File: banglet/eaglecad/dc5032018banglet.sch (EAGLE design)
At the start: 41 parts, among them Q3 DMG3415U-7, U2 AP2112(3.3V), U3 MCP73831T-2ACI/OT, U4 CP2104, X1 32.768, X2 JSTPH, X4 20329

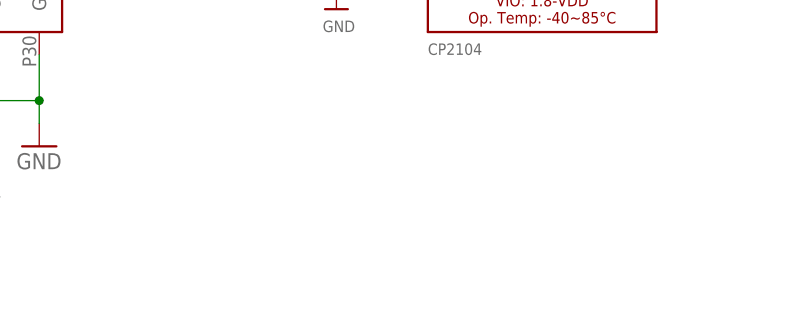
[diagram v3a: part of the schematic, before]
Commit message: add 2 fiducials
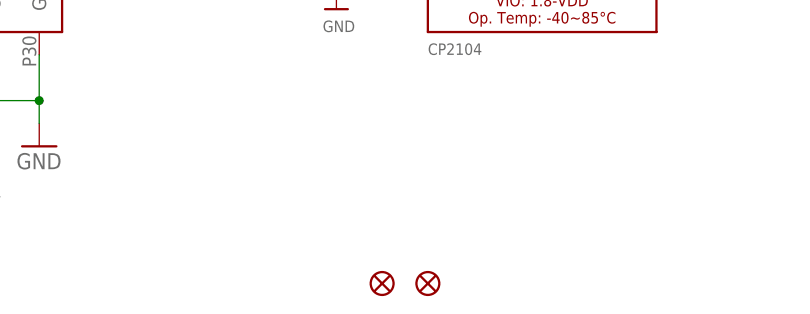
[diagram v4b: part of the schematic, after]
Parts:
- added FD1, FD2: FIDUCIALUFIDUCIAL, SparkFun-Aesthetics:FIDUCIALUFIDUCIAL
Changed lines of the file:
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@@
 <part name="C4" library="SparkFun-Capacitors" library_urn="urn:adsk.eagle:library:510" deviceset="22PF" device="-0603-50V-5%" package3d_urn="urn:adsk.eagle:package:37414/1" value="22pF"/>
 <part name="C2" library="SparkFun-Capacitors" library_urn="urn:adsk.eagle:library:510" deviceset="22PF" device="-0603-50V-5%" package3d_urn="urn:adsk.eagle:package:37414/1" value="22pF"/>
+<part name="FD1" library="SparkFun-Aesthetics" library_urn="urn:adsk.eagle:library:507" deviceset="FIDUCIAL" device="UFIDUCIAL" package3d_urn="urn:adsk.eagle:package:37111/1"/>
+<part name="FD2" library="SparkFun-Aesthetics" library_urn="urn:adsk.eagle:library:507" deviceset="FIDUCIAL" device="UFIDUCIAL" package3d_urn="urn:adsk.eagle:package:37111/1"/>
 </parts>
 <sheets>
@@
 <instance part="C4" gate="G$1" x="-48.26" y="-27.94"/>
 <instance part="C2" gate="G$1" x="-33.02" y="-27.94"/>
+<instance part="FD1" gate="G$1" x="60.96" y="-60.96"/>
+<instance part="FD2" gate="G$1" x="66.04" y="-60.96"/>
 </instances>
 <busses>

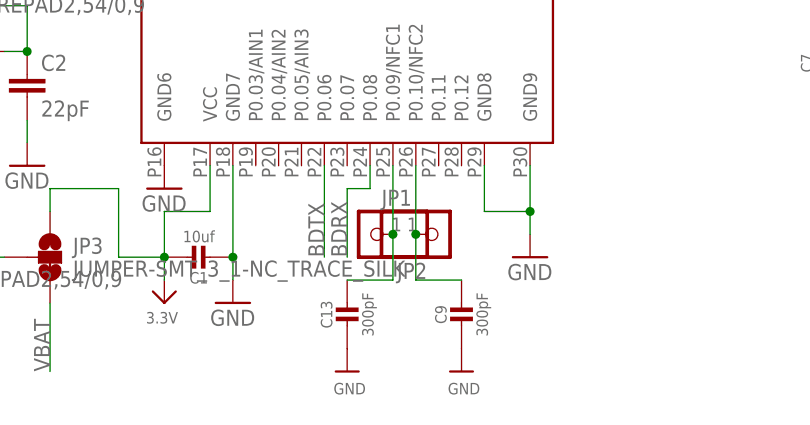
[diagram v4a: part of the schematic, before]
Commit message: removed NFC parts; deleted stray silk
silk still a mess.  I *think* I got all the stray labels.
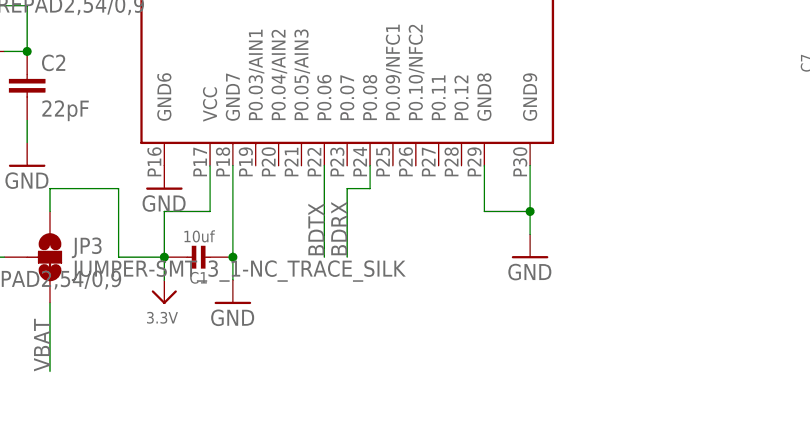
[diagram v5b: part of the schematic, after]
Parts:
- removed C13, C9: 300pF, microbuilder:CAP_CERAMIC_0603MP
- removed JP1, JP2: (no value), microbuilder:HEADER-1X12MM
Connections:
- removed net N$6: C9.1, JP1.1, U1.P0.10/NFC2
- removed net P0.09/NFC1: C13.1, JP2.1, U1.P0.09/NFC1
- net GND: no longer C13.2, C9.2
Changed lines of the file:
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@@
 <part name="GND8" library="supply1" library_urn="urn:adsk.eagle:library:371" deviceset="GND" device=""/>
 <part name="X1" library="adafruit2" deviceset="XTAL" device="-3.2X1.5" value="32.768"/>
-<part name="JP1" library="microbuilder" deviceset="HEADER-1X1" device="2MM"/>
-<part name="JP2" library="microbuilder" deviceset="HEADER-1X1" device="2MM"/>
-<part name="C9" library="microbuilder" deviceset="CAP_CERAMIC" device="_0603MP" value="300pF"/>
-<part name="C13" library="microbuilder" deviceset="CAP_CERAMIC" device="_0603MP" value="300pF"/>
-<part name="U$23" library="microbuilder" deviceset="GND" device=""/>
-<part name="U$28" library="microbuilder" deviceset="GND" device=""/>
 <part name="GND14" library="supply1" library_urn="urn:adsk.eagle:library:371" deviceset="GND" device=""/>
 <part name="GND15" library="supply1" library_urn="urn:adsk.eagle:library:371" deviceset="GND" device=""/>
@@
 <instance part="GND8" gate="1" x="-33.02" y="-35.56"/>
 <instance part="X1" gate="G$1" x="-40.64" y="-22.86"/>
-<instance part="JP1" gate="G$1" x="12.7" y="-43.18"/>
-<instance part="JP2" gate="G$1" x="5.08" y="-43.18" rot="R180"/>
-<instance part="C9" gate="G$1" x="15.24" y="-53.34"/>
-<instance part="C13" gate="G$1" x="2.54" y="-53.34"/>
-<instance part="U$23" gate="G$1" x="2.54" y="-58.42"/>
-<instance part="U$28" gate="G$1" x="15.24" y="-58.42"/>
 <instance part="GND14" gate="1" x="38.1" y="25.4" rot="R90"/>
 <instance part="GND15" gate="1" x="22.86" y="-45.72"/>
@@
 <wire x1="-10.16" y1="-45.72" x2="-10.16" y2="-35.56" width="0.1524" layer="91"/>
 <junction x="-10.16" y="-45.72"/>
-</segment>
-<segment>
-<pinref part="C13" gate="G$1" pin="2"/>
-<pinref part="U$23" gate="G$1" pin="GND"/>
-</segment>
-<segment>
-<pinref part="C9" gate="G$1" pin="2"/>
-<pinref part="U$28" gate="G$1" pin="GND"/>
 </segment>
 <segment>
@@
 </segment>
 </net>
-<net name="P0.09/NFC1" class="0">
-<segment>
-<pinref part="JP2" gate="G$1" pin="1"/>
-<pinref part="C13" gate="G$1" pin="1"/>
-<wire x1="2.54" y1="-48.26" x2="7.62" y2="-48.26" width="0.1524" layer="91"/>
-<wire x1="7.62" y1="-48.26" x2="7.62" y2="-43.18" width="0.1524" layer="91"/>
-<pinref part="U1" gate="G$1" pin="P0.09/NFC1"/>
-<wire x1="7.62" y1="-43.18" x2="7.62" y2="-35.56" width="0.1524" layer="91"/>
-<junction x="7.62" y="-43.18"/>
-</segment>
-</net>
 <net name="TRACED0" class="0">
 <segment>
@@
 </segment>
 </net>
-<net name="N$6" class="0">
-<segment>
-<pinref part="U1" gate="G$1" pin="P0.10/NFC2"/>
-<pinref part="JP1" gate="G$1" pin="1"/>
-<wire x1="10.16" y1="-35.56" x2="10.16" y2="-43.18" width="0.1524" layer="91"/>
-<pinref part="C9" gate="G$1" pin="1"/>
-<wire x1="15.24" y1="-48.26" x2="10.16" y2="-48.26" width="0.1524" layer="91"/>
-<wire x1="10.16" y1="-48.26" x2="10.16" y2="-43.18" width="0.1524" layer="91"/>
-<junction x="10.16" y="-43.18"/>
-</segment>
-</net>

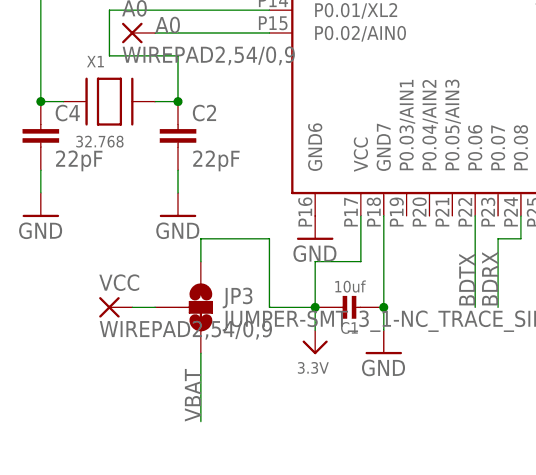
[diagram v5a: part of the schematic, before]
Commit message: make label for LED strip a little clearer
Move two vias away from bmd pads
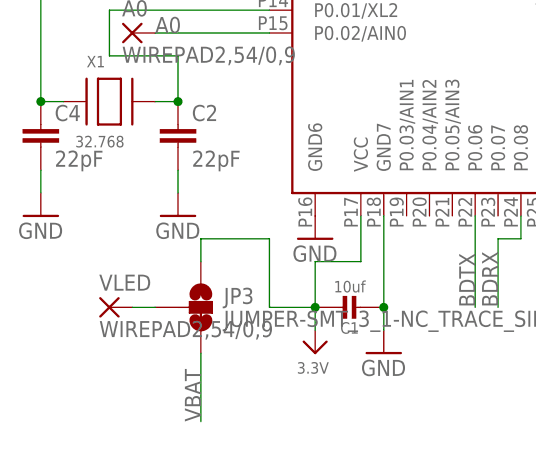
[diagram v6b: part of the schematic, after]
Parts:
- renumbered VCC to VLED
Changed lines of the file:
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@@
 <part name="GND15" library="supply1" library_urn="urn:adsk.eagle:library:371" deviceset="GND" device=""/>
 <part name="A0" library="wirepad" library_urn="urn:adsk.eagle:library:412" deviceset="WIREPAD" device="2,54/0,9"/>
-<part name="VCC" library="wirepad" library_urn="urn:adsk.eagle:library:412" deviceset="WIREPAD" device="2,54/0,9"/>
+<part name="VLED" library="wirepad" library_urn="urn:adsk.eagle:library:412" deviceset="WIREPAD" device="2,54/0,9"/>
 <part name="GND" library="wirepad" library_urn="urn:adsk.eagle:library:412" deviceset="WIREPAD" device="2,54/0,9"/>
 <part name="X4" library="microbuilder" deviceset="MICRO-USB-SMD-B-(10118193-0001LF)-ADASYM" device="" value="20329"/>
@@
 <instance part="GND15" gate="1" x="22.86" y="-45.72"/>
 <instance part="A0" gate="G$1" x="-38.1" y="-15.24"/>
-<instance part="VCC" gate="G$1" x="-40.64" y="-45.72"/>
+<instance part="VLED" gate="G$1" x="-40.64" y="-45.72"/>
 <instance part="GND" gate="G$1" x="-45.72" y="10.16"/>
 <instance part="X4" gate="G$1" x="104.14" y="68.58" rot="R270"/>
@@
 <net name="N$3" class="0">
 <segment>
-<pinref part="VCC" gate="G$1" pin="P"/>
+<pinref part="VLED" gate="G$1" pin="P"/>
 <pinref part="JP3" gate="G$1" pin="2"/>
 <wire x1="-38.1" y1="-45.72" x2="-35.56" y2="-45.72" width="0.1524" layer="91"/>

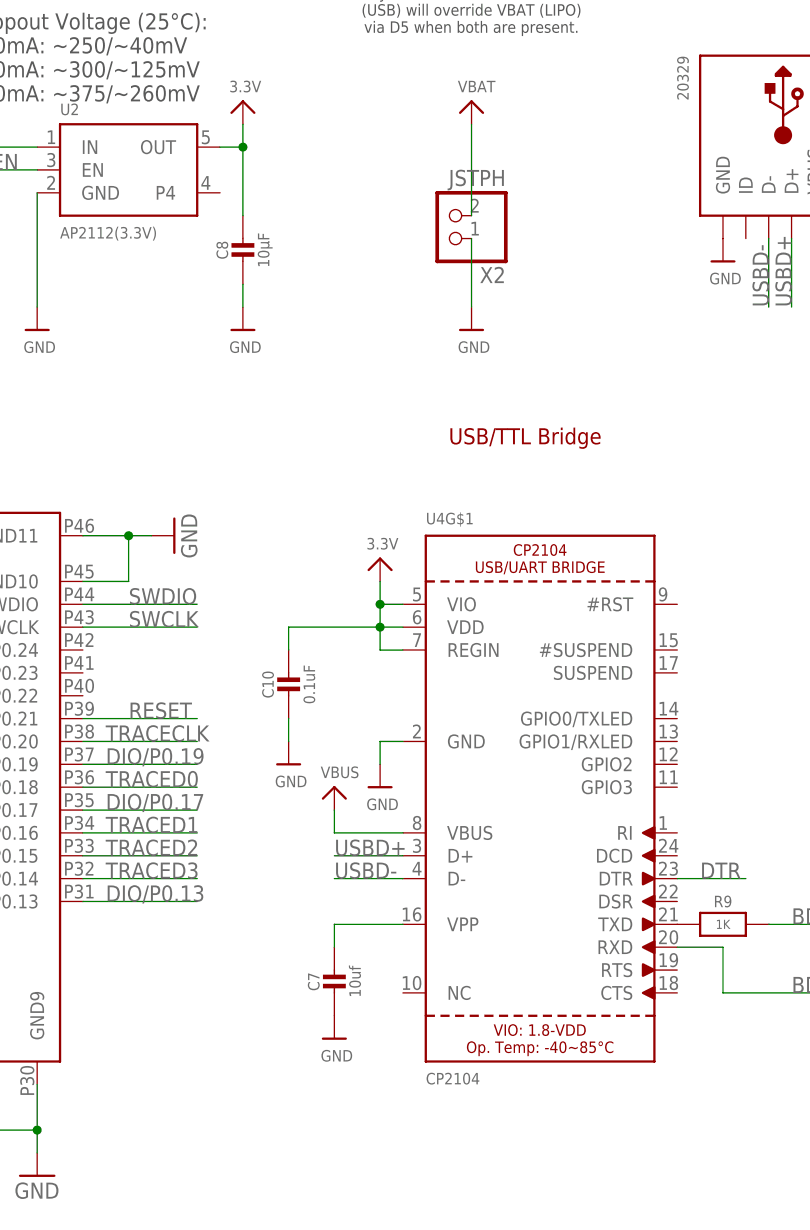
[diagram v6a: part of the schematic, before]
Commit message: Removed cap and replaced JST connector with vias
VPP on the UART is for a one time ROM programming of the UART
which we don't need, so removing it.

We were unable to find batteries that came with the JST female
connectors that went with the used board mounted connector.
Replacing it with vias to use with either board mounted breakaway
header or something else which will fit.

Signed-off-by: nisha <nishakumarx@gmail.com>
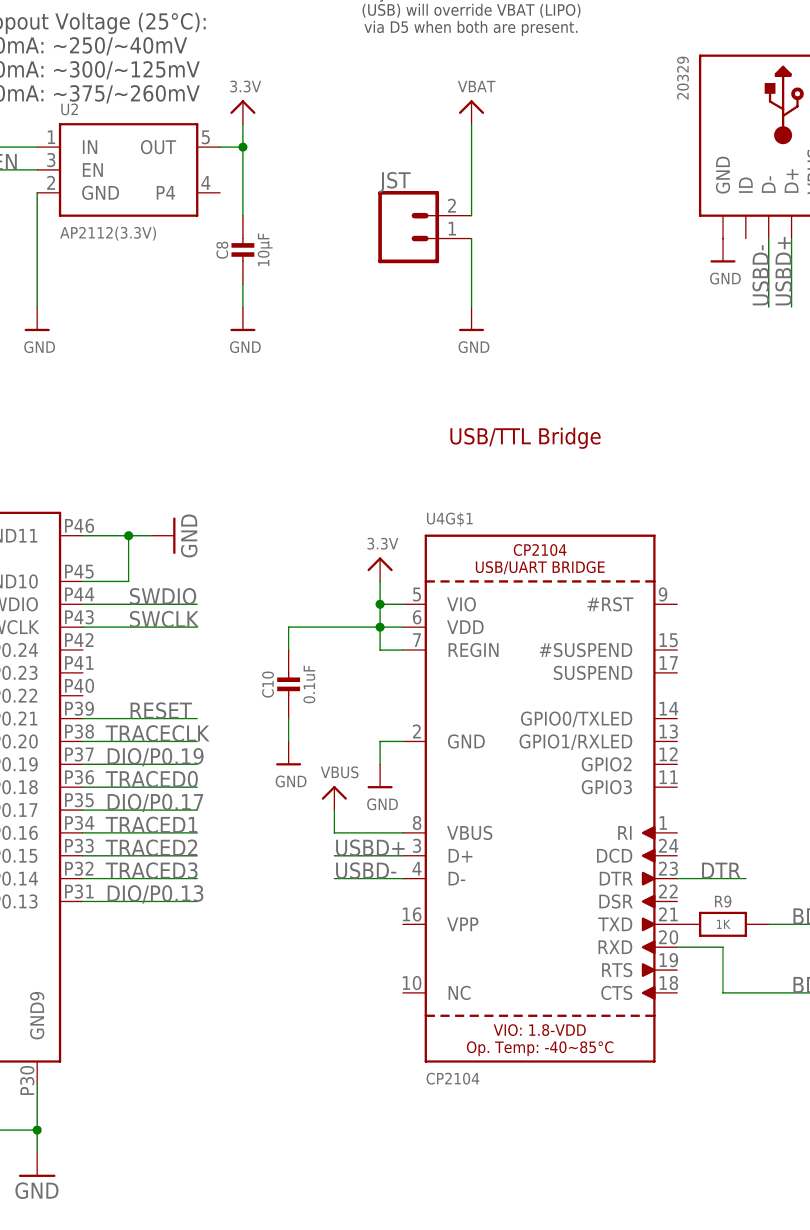
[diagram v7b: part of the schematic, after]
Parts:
- removed C7: 10uf, microbuilder:CAP_CERAMIC0805-NOOUTLINE
- removed X2: JSTPH, microbuilder:CON_JST_PH_2PIN
- added JST: (no value), SparkFun-Connectors:CONN_02
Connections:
- removed net N$14: C7.1, U4G$1.VPP
- net GND: now also JST.1; no longer C7.2, X2.1
- net VBAT: now also JST.2; no longer X2.2
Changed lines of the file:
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@@
 <part name="R12" library="microbuilder" deviceset="RESISTOR" device="_0603_NOOUT" value="100k"/>
 <part name="U$44" library="microbuilder" deviceset="GND" device=""/>
-<part name="X2" library="microbuilder" deviceset="CON_JST_PH_2PIN" device="" value="JSTPH"/>
 <part name="U$16" library="microbuilder" deviceset="VBAT" device=""/>
 <part name="U$22" library="microbuilder" deviceset="GND" device=""/>
@@
 <part name="U$31" library="microbuilder" deviceset="VBUS" device=""/>
 <part name="R9" library="microbuilder" deviceset="RESISTOR" device="_0603_NOOUT" value="1K"/>
-<part name="C7" library="microbuilder" deviceset="CAP_CERAMIC" device="0805-NOOUTLINE" value="10uf"/>
-<part name="U$15" library="microbuilder" deviceset="GND" device=""/>
 <part name="SWD" library="SparkFun-Connectors" deviceset="M04" device="LOCK"/>
 <part name="U1" library="BMD-300" deviceset="BMD-300" device=""/>
@@
 <part name="FD1" library="SparkFun-Aesthetics" library_urn="urn:adsk.eagle:library:507" deviceset="FIDUCIAL" device="UFIDUCIAL" package3d_urn="urn:adsk.eagle:package:37111/1"/>
 <part name="FD2" library="SparkFun-Aesthetics" library_urn="urn:adsk.eagle:library:507" deviceset="FIDUCIAL" device="UFIDUCIAL" package3d_urn="urn:adsk.eagle:package:37111/1"/>
+<part name="JST" library="SparkFun-Connectors" library_urn="urn:adsk.eagle:library:513" deviceset="CONN_02" device="" package3d_urn="urn:adsk.eagle:package:38039/1"/>
 </parts>
 <sheets>
@@
 <instance part="R12" gate="G$1" x="-10.16" y="60.96" rot="R90"/>
 <instance part="U$44" gate="G$1" x="-10.16" y="48.26"/>
-<instance part="X2" gate="G$1" x="68.58" y="60.96" rot="R180"/>
 <instance part="U$16" gate="G$1" x="71.12" y="73.66"/>
 <instance part="U$22" gate="G$1" x="71.12" y="48.26"/>
@@
 <instance part="U$31" gate="G$1" x="55.88" y="-2.54"/>
 <instance part="R9" gate="G$1" x="99.06" y="-17.78"/>
-<instance part="C7" gate="G$1" x="55.88" y="-25.4"/>
-<instance part="U$15" gate="G$1" x="55.88" y="-30.48"/>
 <instance part="SWD" gate="G$1" x="137.16" y="-15.24"/>
 <instance part="U1" gate="G$1" x="2.54" y="7.62"/>
@@
 <instance part="FD1" gate="G$1" x="60.96" y="-60.96"/>
 <instance part="FD2" gate="G$1" x="66.04" y="-60.96"/>
+<instance part="JST" gate="G$1" x="63.5" y="58.42"/>
 </instances>
 <busses>
@@
 </segment>
 <segment>
-<pinref part="X2" gate="G$1" pin="1"/>
 <pinref part="U$22" gate="G$1" pin="GND"/>
 <wire x1="71.12" y1="50.8" x2="71.12" y2="58.42" width="0.1524" layer="91"/>
+<pinref part="JST" gate="G$1" pin="1"/>
 </segment>
 <segment>
@@
 <pinref part="U$24" gate="G$1" pin="GND"/>
 <wire x1="50.8" y1="5.08" x2="50.8" y2="2.54" width="0.1524" layer="91"/>
-</segment>
-<segment>
-<pinref part="C7" gate="G$1" pin="2"/>
-<pinref part="U$15" gate="G$1" pin="GND"/>
 </segment>
 <segment>
@@
 </segment>
 <segment>
-<pinref part="X2" gate="G$1" pin="2"/>
 <pinref part="U$16" gate="G$1" pin="VBAT"/>
 <wire x1="71.12" y1="71.12" x2="71.12" y2="60.96" width="0.1524" layer="91"/>
+<pinref part="JST" gate="G$1" pin="2"/>
 </segment>
 <segment>
@@
 </segment>
 </net>
-<net name="N$14" class="1">
-<segment>
-<pinref part="U4" gate="G$1" pin="VPP"/>
-<pinref part="C7" gate="G$1" pin="1"/>
-<wire x1="63.5" y1="-17.78" x2="55.88" y2="-17.78" width="0.1524" layer="91"/>
-<wire x1="55.88" y1="-17.78" x2="55.88" y2="-20.32" width="0.1524" layer="91"/>
-</segment>
-</net>

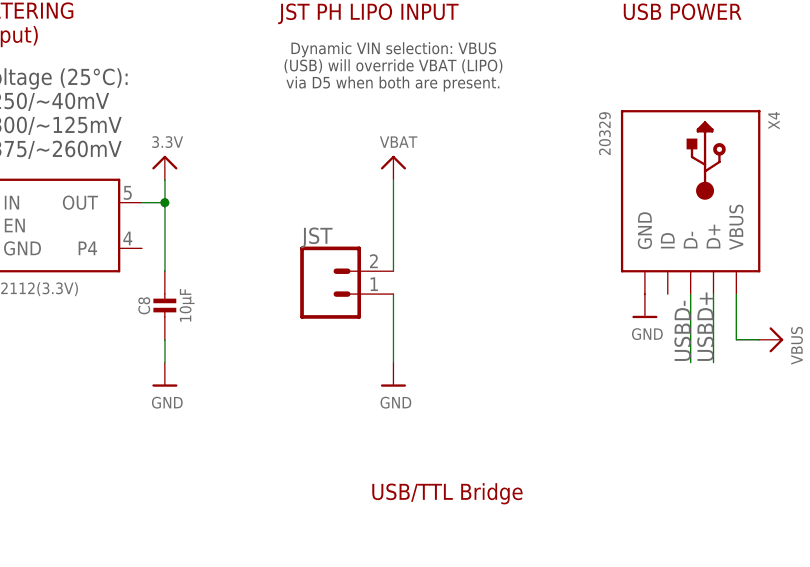
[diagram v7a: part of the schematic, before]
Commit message: Add banlet lib with 2.5mm part and use as J1
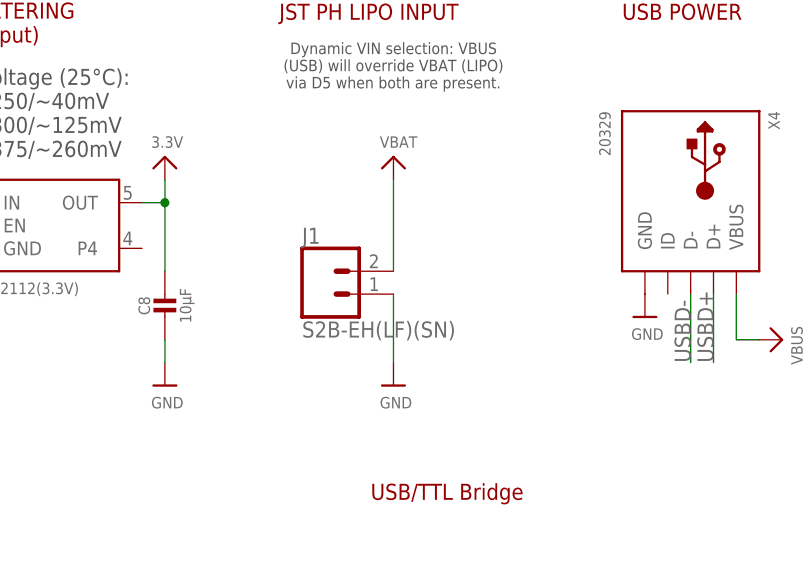
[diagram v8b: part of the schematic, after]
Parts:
- removed JST: (no value), SparkFun-Connectors:CONN_02
- added J1: S2B-EH(LF)(SN), banglet:S2B-EH(LF)(SN)
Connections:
- net GND: now also J1.1; no longer JST.1
- net VBAT: now also J1.2; no longer JST.2
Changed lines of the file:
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@@
 <part name="FD1" library="SparkFun-Aesthetics" library_urn="urn:adsk.eagle:library:507" deviceset="FIDUCIAL" device="UFIDUCIAL" package3d_urn="urn:adsk.eagle:package:37111/1"/>
 <part name="FD2" library="SparkFun-Aesthetics" library_urn="urn:adsk.eagle:library:507" deviceset="FIDUCIAL" device="UFIDUCIAL" package3d_urn="urn:adsk.eagle:package:37111/1"/>
-<part name="JST" library="SparkFun-Connectors" library_urn="urn:adsk.eagle:library:513" deviceset="CONN_02" device="" package3d_urn="urn:adsk.eagle:package:38039/1"/>
+<part name="J1" library="banglet" deviceset="S2B-EH(LF)(SN)" device=""/>
 </parts>
 <sheets>
@@
 <instance part="FD1" gate="G$1" x="60.96" y="-60.96"/>
 <instance part="FD2" gate="G$1" x="66.04" y="-60.96"/>
-<instance part="JST" gate="G$1" x="63.5" y="58.42"/>
+<instance part="J1" gate="G$1" x="63.5" y="58.42"/>
 </instances>
 <busses>
@@
 <pinref part="U$22" gate="G$1" pin="GND"/>
 <wire x1="71.12" y1="50.8" x2="71.12" y2="58.42" width="0.1524" layer="91"/>
-<pinref part="JST" gate="G$1" pin="1"/>
+<pinref part="J1" gate="G$1" pin="1"/>
 </segment>
 <segment>
@@
 <pinref part="U$16" gate="G$1" pin="VBAT"/>
 <wire x1="71.12" y1="71.12" x2="71.12" y2="60.96" width="0.1524" layer="91"/>
-<pinref part="JST" gate="G$1" pin="2"/>
-</segment>
-<segment>
+<pinref part="J1" gate="G$1" pin="2"/>
+</segment>
+<segment>
